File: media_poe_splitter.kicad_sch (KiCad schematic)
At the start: 76 parts, among them IC1 LAN7850-I_8JX, IC2 17791063215, IC3 93AA66C-I/SN, J1 Screw_Terminal_01x02, X1 7499811120, X2 68710614522, Y1 830055299

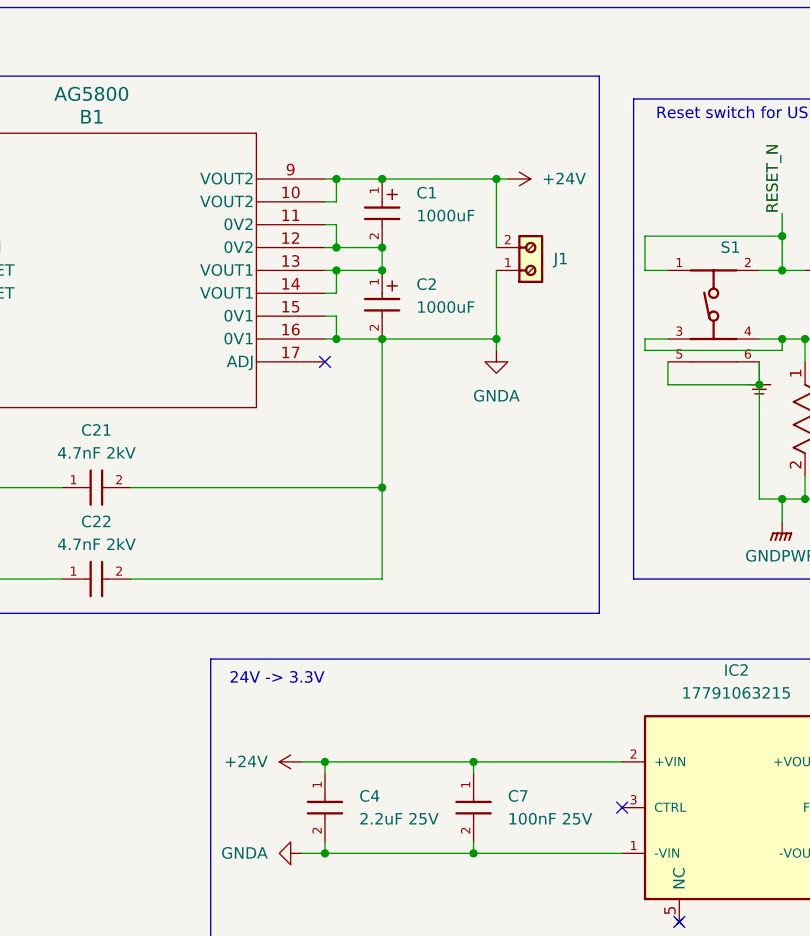
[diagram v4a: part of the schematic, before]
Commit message: poe splitter: transform output to be in series to allow switching it off
Signed-off-by: Marc 'risson' Schmitt <marc.schmitt@risson.space>
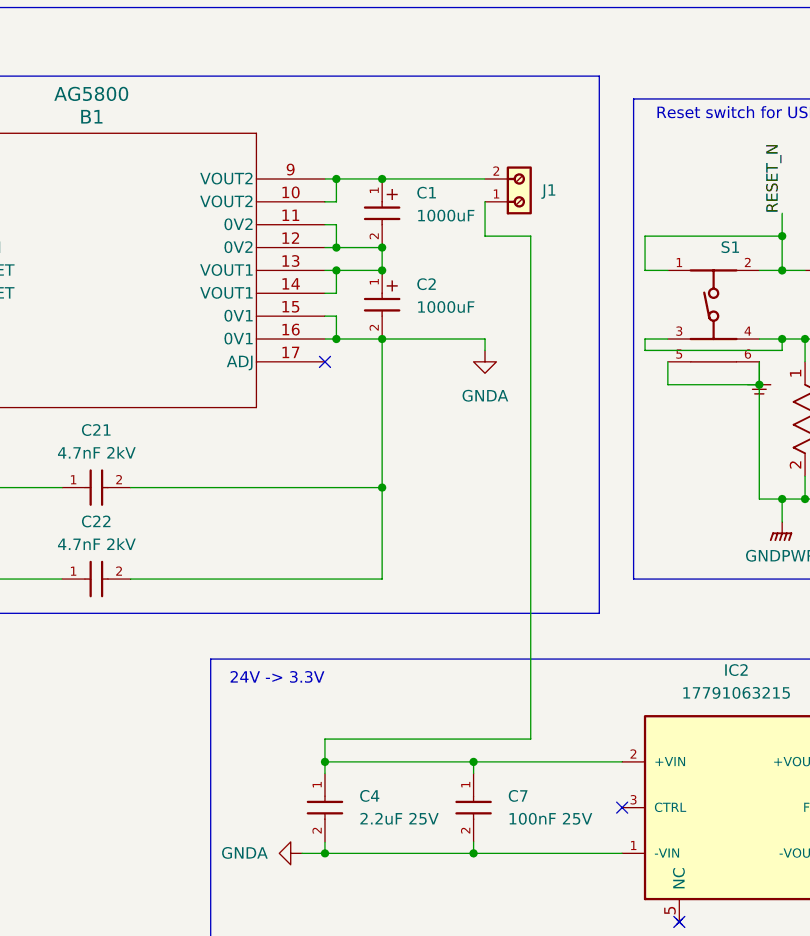
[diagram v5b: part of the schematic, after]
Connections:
- net GNDA: no longer J1.1
- net +24V: no longer names the net of B1.10 (VOUT2), B1.9 (VOUT2), C1.1, J1.2
- net +24V: no longer C4.1, C7.1, IC2.2 (+VIN)
- new net: C4.1, C7.1, IC2.2 (+VIN), J1.1
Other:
- moved on the sheet: J1
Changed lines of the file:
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@@
 	)
 	(junction
-		(at 269.24 229.87)
-		(diameter 0)
-		(color 0 0 0 0)
-	)
-	(junction
 		(at 359.41 238.76)
 		(diameter 0)
@@
 	)
 	(junction
-		(at 269.24 212.09)
-		(diameter 0)
-		(color 0 0 0 0)
-	)
-	(junction
 		(at 314.96 152.4)
 		(diameter 0)
@@
 	(wire
 		(pts
+			(xy 273.05 218.44) (xy 273.05 274.32)
+		)
+		(stroke
+			(width 0)
+			(type default)
+		)
+	)
+	(wire
+		(pts
 			(xy 247.65 287.02) (xy 250.19 287.02)
 		)
@@
 	(wire
 		(pts
-			(xy 269.24 212.09) (xy 270.51 212.09)
+			(xy 251.46 219.71) (xy 251.46 217.17)
 		)
 		(stroke
@@
 	(wire
 		(pts
-			(xy 251.46 219.71) (xy 251.46 217.17)
+			(xy 501.65 111.76) (xy 504.19 111.76)
 		)
 		(stroke
@@
 	(wire
 		(pts
-			(xy 501.65 111.76) (xy 504.19 111.76)
+			(xy 214.63 144.78) (xy 214.63 157.48)
 		)
 		(stroke
@@
 	(wire
 		(pts
-			(xy 214.63 144.78) (xy 214.63 157.48)
+			(xy 346.71 219.71) (xy 359.41 219.71)
 		)
 		(stroke
@@
 	(wire
 		(pts
-			(xy 346.71 219.71) (xy 359.41 219.71)
+			(xy 168.91 214.63) (xy 171.45 214.63)
 		)
 		(stroke
@@
 	(wire
 		(pts
-			(xy 168.91 214.63) (xy 171.45 214.63)
+			(xy 250.19 274.32) (xy 250.19 276.86)
 		)
 		(stroke
@@
 	(wire
 		(pts
-			(xy 256.54 212.09) (xy 269.24 212.09)
+			(xy 256.54 212.09) (xy 267.97 212.09)
 		)
 		(stroke
@@
 	(wire
 		(pts
-			(xy 269.24 212.09) (xy 269.24 219.71)
-		)
-		(stroke
-			(width 0)
-			(type default)
-		)
-	)
-	(wire
-		(pts
 			(xy 251.46 224.79) (xy 251.46 222.25)
 		)
@@
 	(wire
 		(pts
-			(xy 256.54 229.87) (xy 269.24 229.87)
+			(xy 256.54 229.87) (xy 267.97 229.87)
 		)
 		(stroke
@@
 	(wire
 		(pts
-			(xy 269.24 229.87) (xy 269.24 222.25)
+			(xy 267.97 214.63) (xy 267.97 218.44)
 		)
 		(stroke
@@
 	(wire
 		(pts
+			(xy 267.97 218.44) (xy 273.05 218.44)
+		)
+		(stroke
+			(width 0)
+			(type default)
+		)
+	)
+	(wire
+		(pts
 			(xy 196.85 246.38) (xy 196.85 214.63)
 		)
@@
 	(wire
 		(pts
+			(xy 273.05 274.32) (xy 250.19 274.32)
+		)
+		(stroke
+			(width 0)
+			(type default)
+		)
+	)
+	(wire
+		(pts
 			(xy 82.55 124.46) (xy 85.09 124.46)
 		)
@@
 	(wire
 		(pts
-			(xy 269.24 229.87) (xy 269.24 231.14)
+			(xy 267.97 229.87) (xy 267.97 231.14)
 		)
 		(stroke
@@
 	(wire
 		(pts
-			(xy 247.65 276.86) (xy 250.19 276.86)
-		)
-		(stroke
-			(width 0)
-			(type default)
-		)
-	)
-	(wire
-		(pts
 			(xy 302.26 152.4) (xy 304.8 152.4)
 		)
@@
 	(symbol
 		(lib_id "power:GNDA")
-		(at 269.24 231.14 0)
+		(at 267.97 231.14 0)
 		(unit 1)
 		(exclude_from_sim no)
@@
 		(fields_autoplaced yes)
 		(property "Reference" "#PWR01"
-			(at 269.24 237.49 0)
+			(at 267.97 237.49 0)
 			(effects
 				(font
@@
 		)
 		(property "Value" "GNDA"
-			(at 269.24 236.22 0)
+			(at 267.97 236.22 0)
 			(effects
 				(font
@@
 		)
 		(property "Footprint" ""
-			(at 269.24 231.14 0)
+			(at 267.97 231.14 0)
 			(effects
 				(font
@@
 		)
 		(property "Datasheet" ""
-			(at 269.24 231.14 0)
+			(at 267.97 231.14 0)
 			(effects
 				(font
@@
 		)
 		(property "Description" "Power symbol creates a global label with name \"GNDA\" , analog ground"
-			(at 269.24 231.14 0)
+			(at 267.97 231.14 0)
 			(effects
 				(font
@@
 	)
 	(symbol
-		(lib_id "power:+24V")
-		(at 247.65 276.86 90)
-		(unit 1)
-		(exclude_from_sim no)
-		(in_bom yes)
-		(on_board yes)
-		(dnp no)
-		(fields_autoplaced yes)
-		(property "Reference" "#PWR08"
-			(at 251.46 276.86 0)
-			(effects
-				(font
-					(size 1.27 1.27)
-				)
-				(hide yes)
-			)
-		)
-		(property "Value" "+24V"
-			(at 243.84 276.8599 90)
-			(effects
-				(font
-					(size 1.27 1.27)
-				)
-				(justify left)
-			)
-		)
-		(property "Footprint" ""
-			(at 247.65 276.86 0)
-			(effects
-				(font
-					(size 1.27 1.27)
-				)
-				(hide yes)
-			)
-		)
-		(property "Datasheet" ""
-			(at 247.65 276.86 0)
-			(effects
-				(font
-					(size 1.27 1.27)
-				)
-				(hide yes)
-			)
-		)
-		(property "Description" "Power symbol creates a global label with name \"+24V\""
-			(at 247.65 276.86 0)
-			(effects
-				(font
-					(size 1.27 1.27)
-				)
-				(hide yes)
-			)
-		)
-		(pin "1"
-		)
-		(instances
-			(project "media_poe_splitter"
-				(path "/6322d6ab-712b-4593-ad2b-135ce593cd38"
-					(reference "#PWR08")
-					(unit 1)
-				)
-			)
-		)
-	)
-	(symbol
 		(lib_id "power:+1V2")
 		(at 321.31 154.94 90)
@@
 	)
 	(symbol
-		(lib_id "power:+24V")
-		(at 270.51 212.09 270)
-		(unit 1)
-		(exclude_from_sim no)
-		(in_bom yes)
-		(on_board yes)
-		(dnp no)
-		(fields_autoplaced yes)
-		(property "Reference" "#PWR02"
-			(at 266.7 212.09 0)
-			(effects
-				(font
-					(size 1.27 1.27)
-				)
-				(hide yes)
-			)
-		)
-		(property "Value" "+24V"
-			(at 274.32 212.0899 90)
-			(effects
-				(font
-					(size 1.27 1.27)
-				)
-				(justify left)
-			)
-		)
-		(property "Footprint" ""
-			(at 270.51 212.09 0)
-			(effects
-				(font
-					(size 1.27 1.27)
-				)
-				(hide yes)
-			)
-		)
-		(property "Datasheet" ""
-			(at 270.51 212.09 0)
-			(effects
-				(font
-					(size 1.27 1.27)
-				)
-				(hide yes)
-			)
-		)
-		(property "Description" "Power symbol creates a global label with name \"+24V\""
-			(at 270.51 212.09 0)
-			(effects
-				(font
-					(size 1.27 1.27)
-				)
-				(hide yes)
-			)
-		)
-		(pin "1"
-		)
-		(instances
-			(project ""
-				(path "/6322d6ab-712b-4593-ad2b-135ce593cd38"
-					(reference "#PWR02")
-					(unit 1)
-				)
-			)
-		)
-	)
-	(symbol
 		(lib_id "power:+1V2")
 		(at 467.36 119.38 270)
@@
 	(symbol
 		(lib_id "691210910002:691210910002")
-		(at 274.32 219.71 270)
+		(at 273.05 212.09 270)
 		(mirror x)
 		(unit 1)
@@
 		(dnp no)
 		(property "Reference" "J1"
-			(at 275.59 220.9801 90)
+			(at 274.32 213.3601 90)
 			(effects
 				(font
@@
 		)
 		(property "Value" "Screw_Terminal_01x02"
-			(at 271.7801 217.17 0)
+			(at 270.5101 209.55 0)
 			(effects
 				(font
@@
 		)
 		(property "Footprint" "691210910002:691210910002"
-			(at 274.32 219.71 0)
+			(at 273.05 212.09 0)
 			(effects
 				(font
@@
 		)
 		(property "Datasheet" "https://www.we-online.com/components/products/datasheet/691210910002.pdf"
-			(at 274.32 219.71 0)
+			(at 273.05 212.09 0)
 			(effects
 				(font
@@
 		)
 		(property "Description" "WR-TBL Series 2109 - Rising Cage Clamp - THT - 2.54mm"
-			(at 274.32 219.71 0)
+			(at 273.05 212.09 0)
 			(effects
 				(font
@@
 		)
 		(property "Mount" "THT"
-			(at 274.32 219.71 0)
+			(at 273.05 212.09 0)
 			(effects
 				(font
@@
 		)
 		(property "MPN" "691210910002"
-			(at 274.32 219.71 0)
+			(at 273.05 212.09 0)
 			(effects
 				(font
@@
 		)
 		(property "Manufacturer" "Wurth Elektronik"
-			(at 274.32 219.71 0)
+			(at 273.05 212.09 0)
 			(effects
 				(font

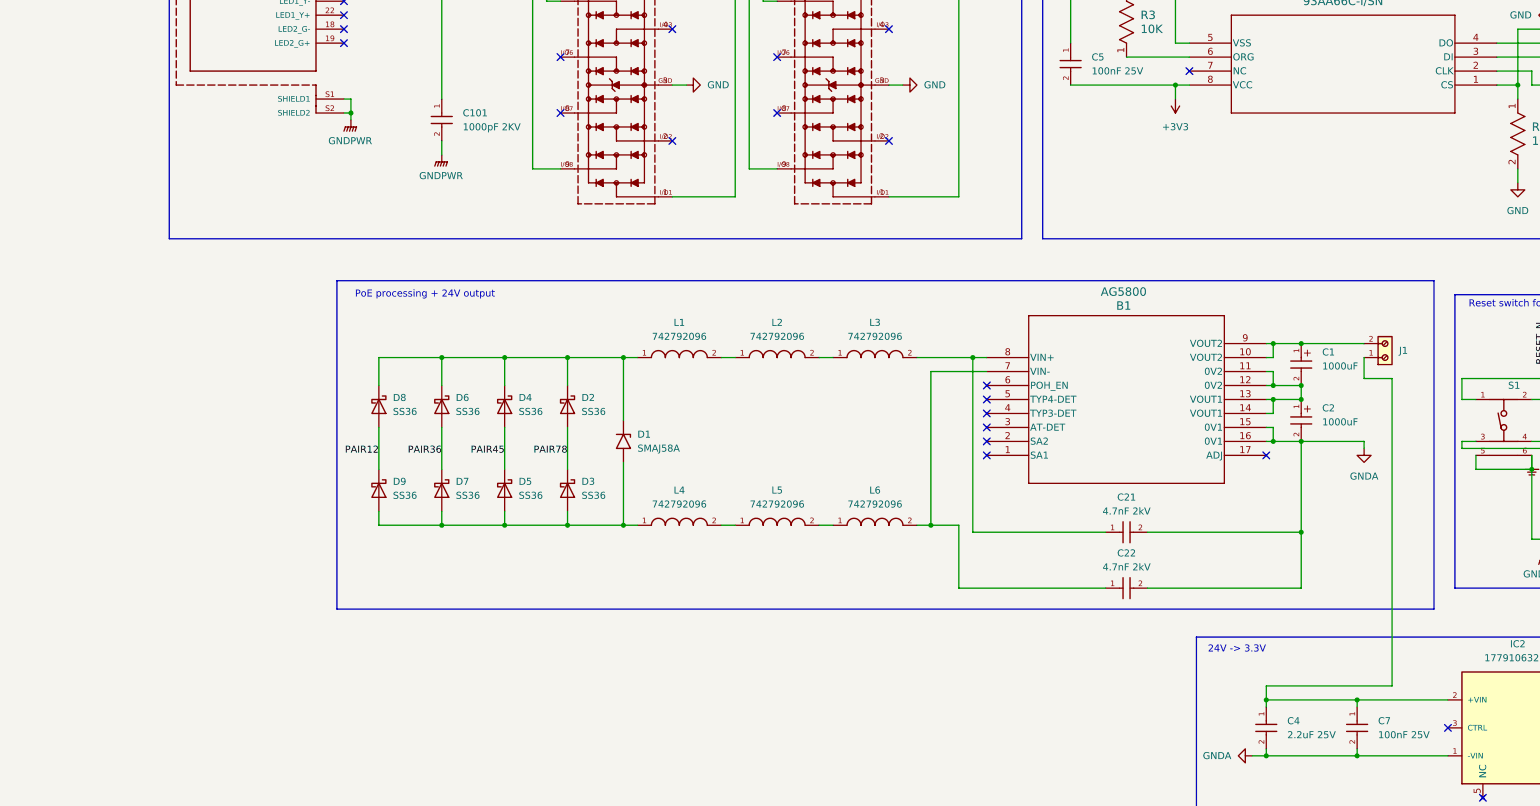
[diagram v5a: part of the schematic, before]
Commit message: Add MOSFET to 24V output for enable/disable capability
Signed-off-by: Marc 'risson' Schmitt <marc.schmitt@risson.space>
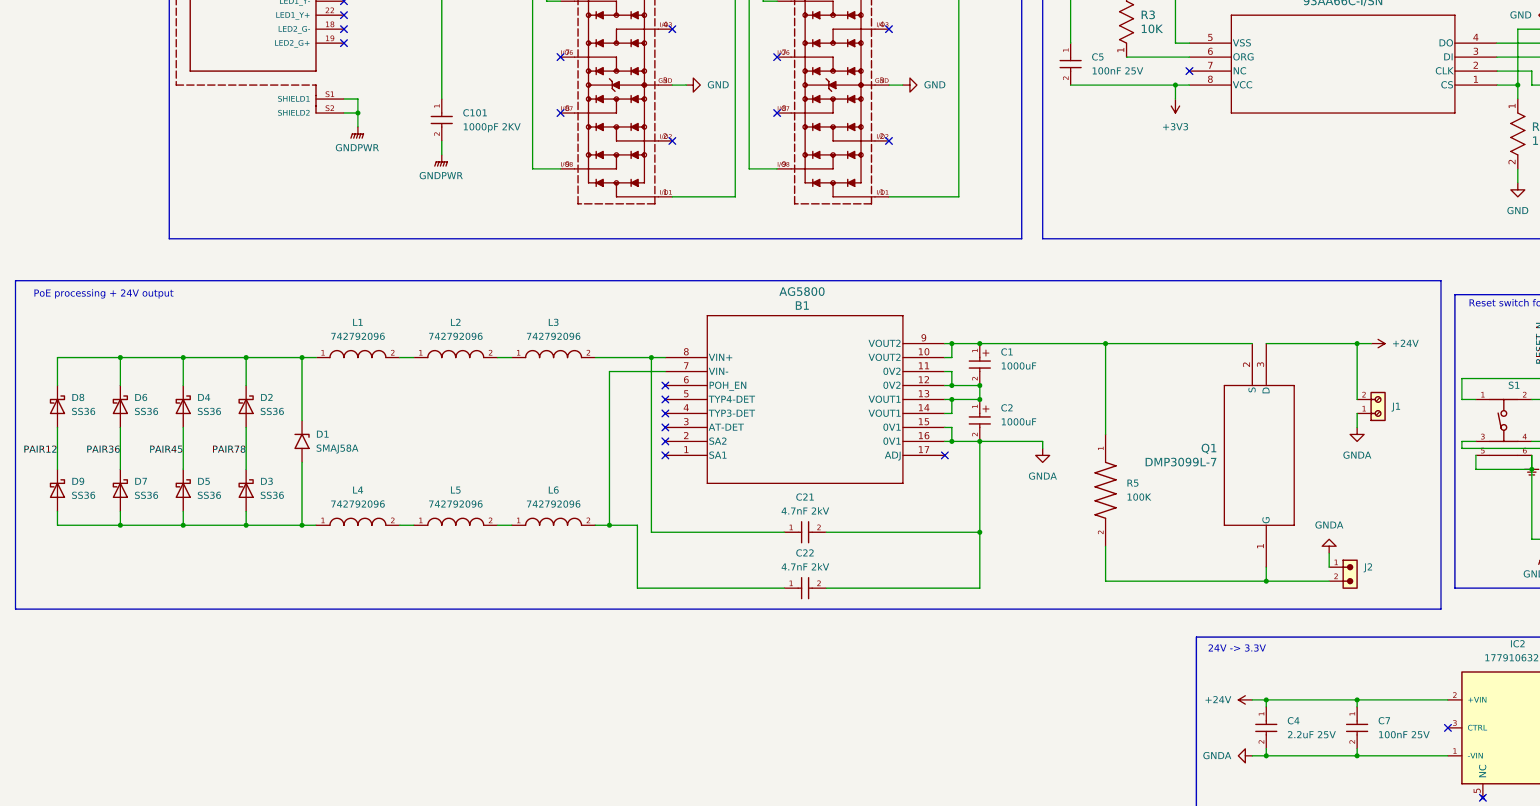
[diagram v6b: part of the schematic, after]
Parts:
- added J2: ~, 61300211121:61300211121, symbol 61300211121:61300211121
- added Q1: DMP3099L-7, DMP3099L-7:DMP3099L-7, symbol DMP3099L-7:DMP3099L-7
- added R5: 100K, RC1206FR-07100KL:RC1206FR-07100KL, symbol RC1206FR-07100KL:RC1206FR-07100KL
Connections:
- net GNDA: now also J1.1, J2.1
- net +24V: now reaches C4.1, C7.1, IC2.2 (+VIN)
- net +24V: now also J1.2, Q1.3 (D); no longer J1.1
- net at B1.10 (VOUT2), B1.9 (VOUT2), C1.1: now also Q1.2 (S), R5.1; no longer J1.2
- new net: J2.2, Q1.1 (G), R5.2
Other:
- moved on the sheet: B1, C1, C2, C21, C22, D1, D2, D3, D4, D5, D6, D7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

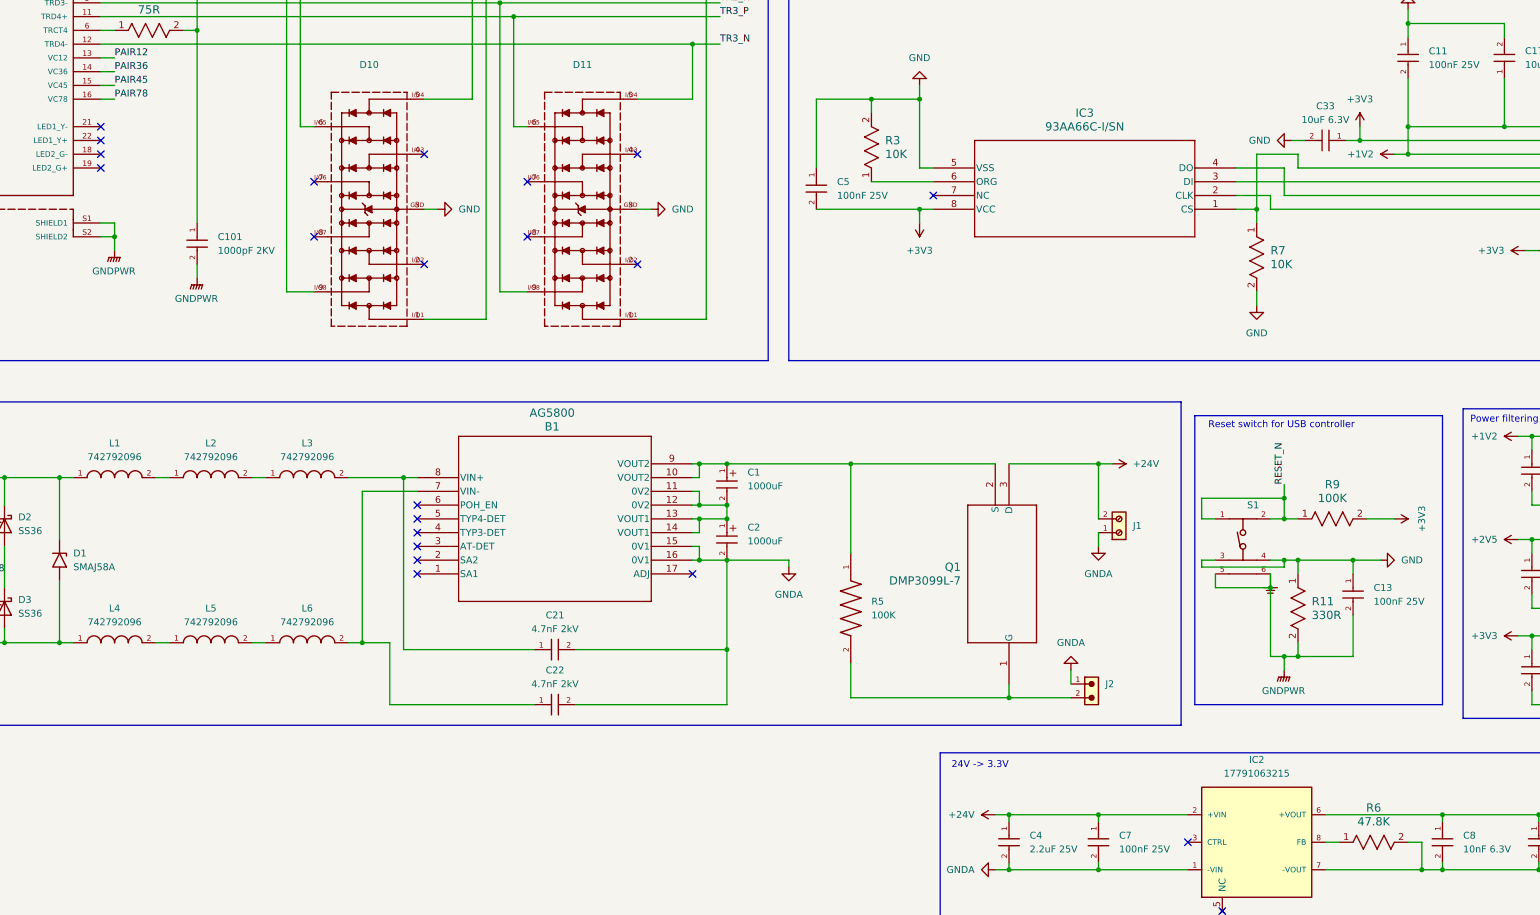
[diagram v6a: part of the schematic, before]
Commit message: Add LEDs for Ethernet monitoring
Signed-off-by: Marc 'risson' Schmitt <marc.schmitt@risson.space>
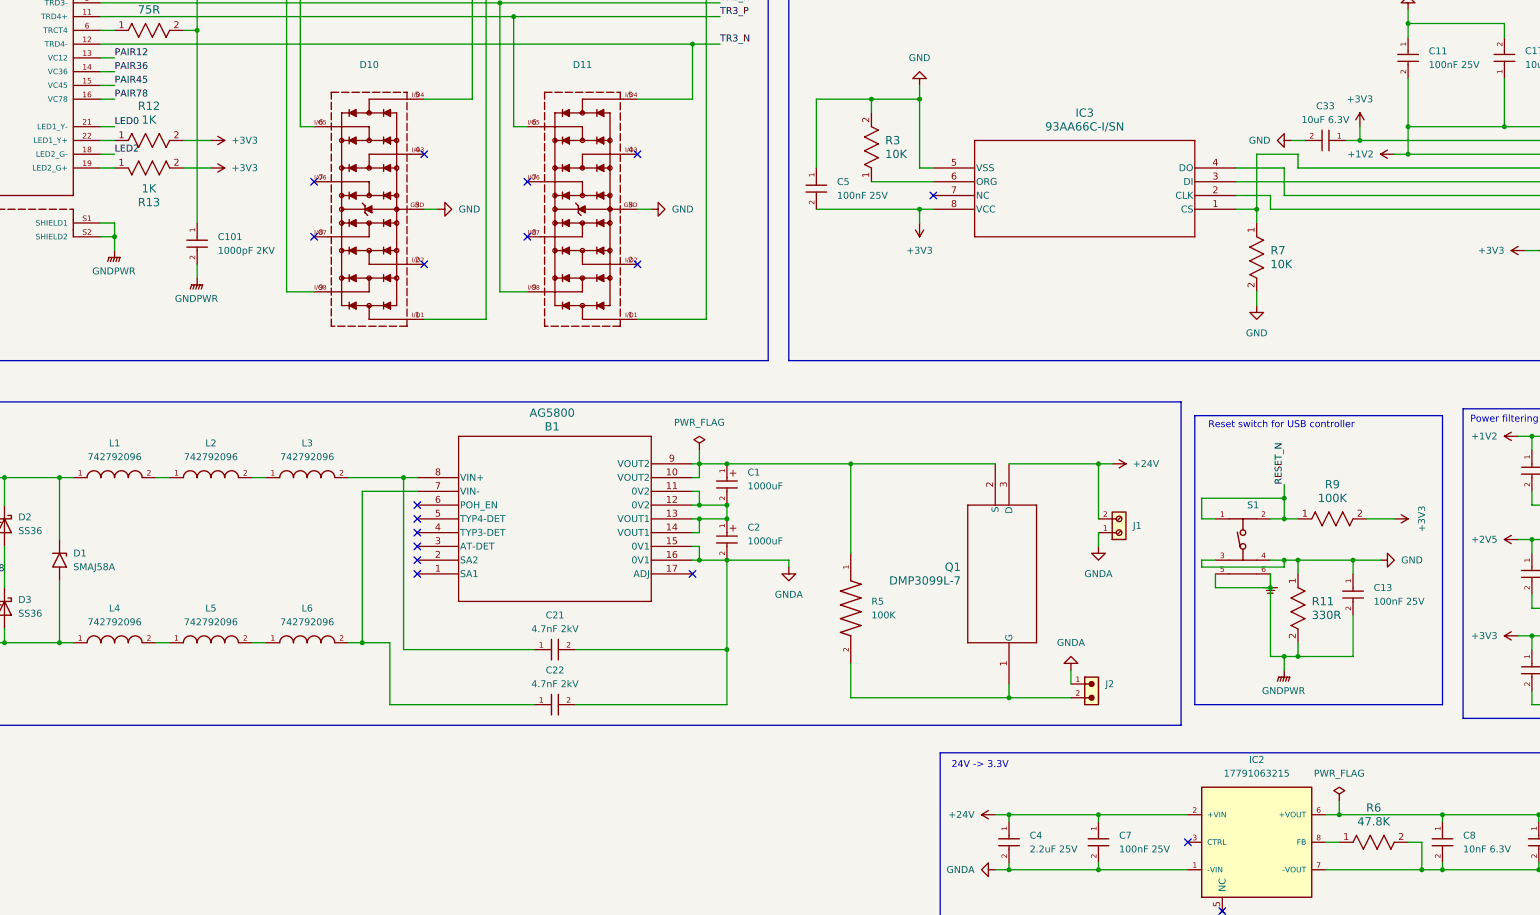
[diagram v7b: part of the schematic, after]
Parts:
- added R12, R13: 1K, RC1206FR-071KL:RC1206FR-071KL, symbol RC1206FR-071KL:RC1206FR-071KL
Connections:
- net +3V3: now also R12.2, R13.2
- net LED0: now also X1.21 (LED1_Y-)
- net LED2: now also X1.18 (LED2_G-)
- net at X1.19 (LED2_G+): now also R13.1
- net at X1.22 (LED1_Y+): now also R12.1
- no-connect marks 39 -> 35
